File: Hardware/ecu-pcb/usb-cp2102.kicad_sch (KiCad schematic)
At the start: 17 parts

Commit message: Ecu SCH Ready
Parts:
- gave numbers to parts that had none: 17

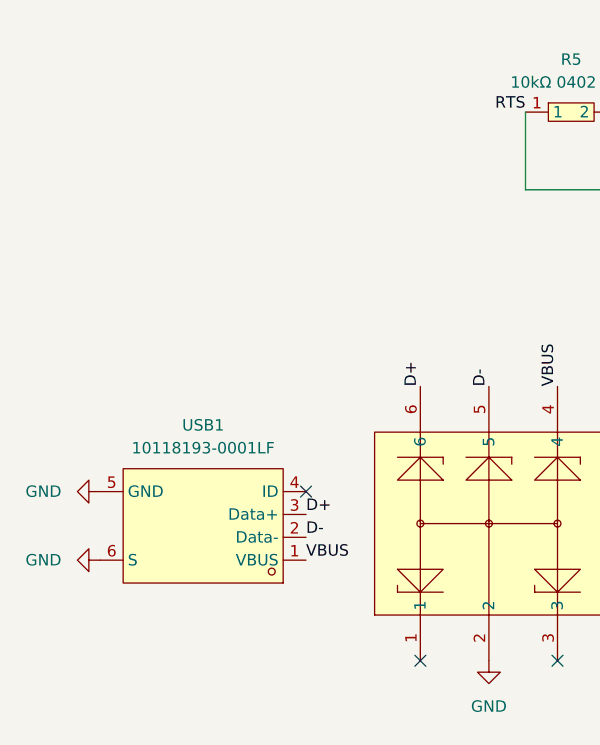
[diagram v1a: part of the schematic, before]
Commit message: Added Vertical USB
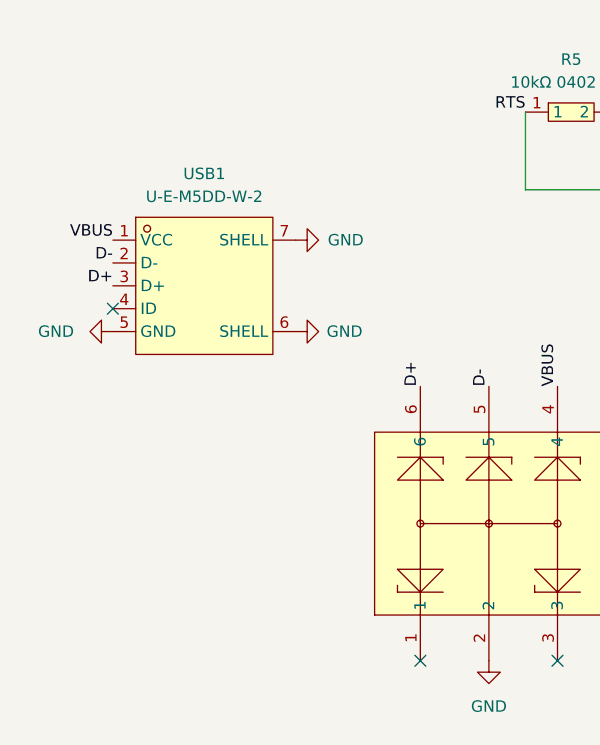
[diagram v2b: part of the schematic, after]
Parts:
- removed USB1: 10118193-0001LF, easyeda2kicad:MICRO-USB-SMD_10118193-0001LF, symbol easyeda2kicad:10118193-0001LF
- added USB1: U-E-M5DD-W-2, easyeda2kicad:MICRO-USB-TH_U-E-M5DD-W-2, symbol easyeda2kicad:U-E-M5DD-W-2
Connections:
- net D+: now also USB1.3 (D+)
- net D-: now also USB1.2 (D-)
- net GND: now also USB1.5 (GND), USB1.6 (SHELL), USB1.7 (SHELL)
- net VBUS: now also USB1.1 (VCC)
